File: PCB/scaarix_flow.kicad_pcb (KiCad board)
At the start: 2 copper layers, 153.4 x 160 mm, 63 parts

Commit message: Changed footprint and rerouted
Used a different footprint that wasn't hotswappable. Changed it and Re-routed
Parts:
- S1, S10, S11, S12, S13, S14, S15, S16, S17, S18, S19, S2, S20, S21, S22, S23, S24, S27, S3, S4, S5, S6, S7, S8, S9: footprint Erics_Footprints:SW_MX_reversible -> Erics_Footprints:MX_Hotswap
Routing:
- net P21: track 187.2 -> 243.5 mm, vias 0 -> 9
- net P19: track 145.2 -> 199.3 mm, vias 0 -> 5
- net P20: track 166.0 -> 219.2 mm, vias 0 -> 5
- net P18: track 126.8 -> 178.8 mm, vias 0 -> 5
- net P15: track 107.9 -> 159.9 mm, vias 0 -> 5
- net P14: track 89.2 -> 139.3 mm, vias 0 -> 10
- net ring_bottom: track 18.8 -> 44.7 mm, vias 0 -> 1
- net far_bottom: track 18.8 -> 44.7 mm, vias 0 -> 1
- net middle_top: track 18.8 -> 44.7 mm, vias 0 -> 1
- net ring_top: track 18.8 -> 44.7 mm, vias 0 -> 1
- net ring_home: track 18.8 -> 44.7 mm, vias 0 -> 1
- net middle_bottom: track 18.8 -> 44.7 mm, vias 0 -> 1
- net middle_home: track 18.8 -> 44.7 mm, vias 0 -> 1
- net far_home: track 18.8 -> 44.7 mm, vias 0 -> 1
- net far_top: track 18.8 -> 44.7 mm, vias 0 -> 1
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
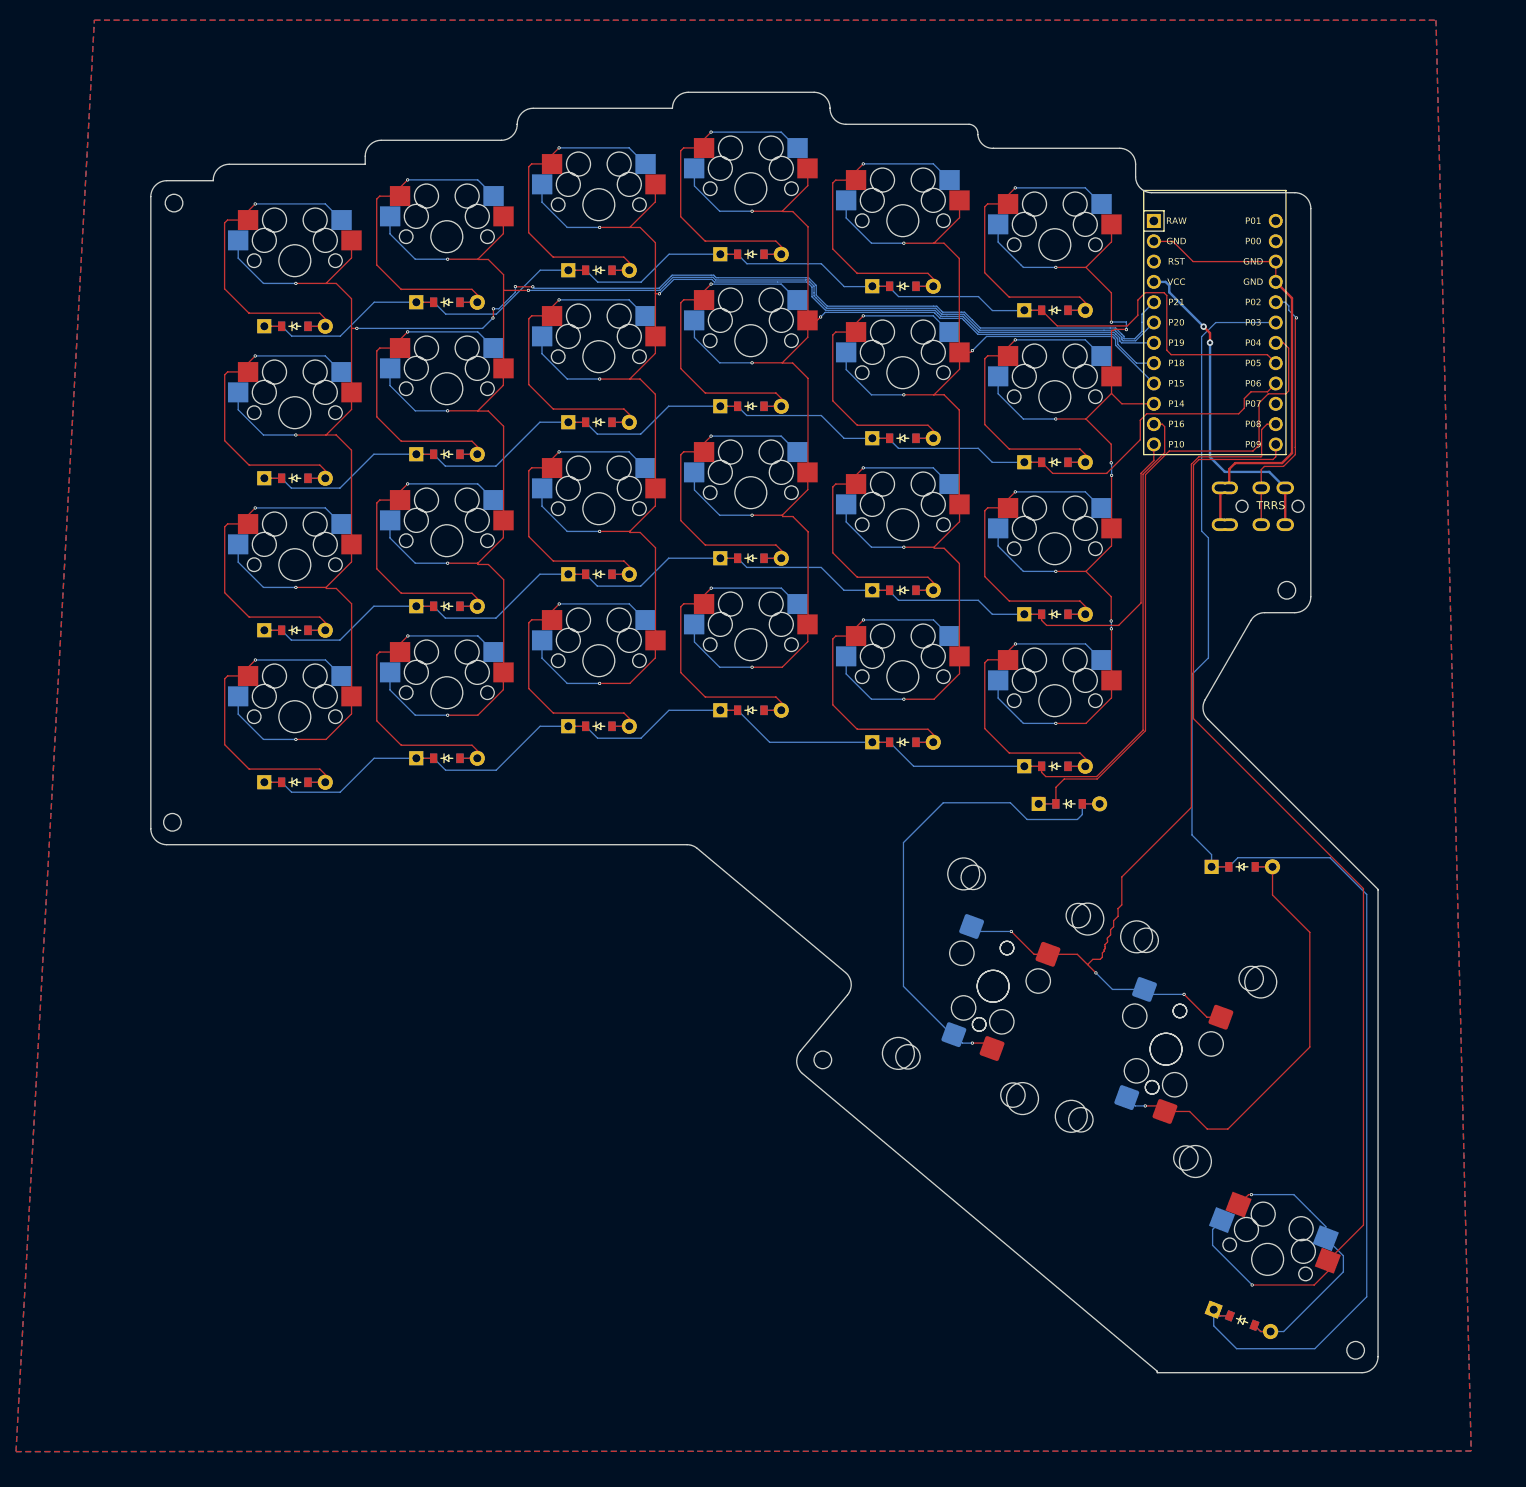
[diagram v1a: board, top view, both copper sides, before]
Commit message: Fixed stabilizers
Stab orientation was wrong
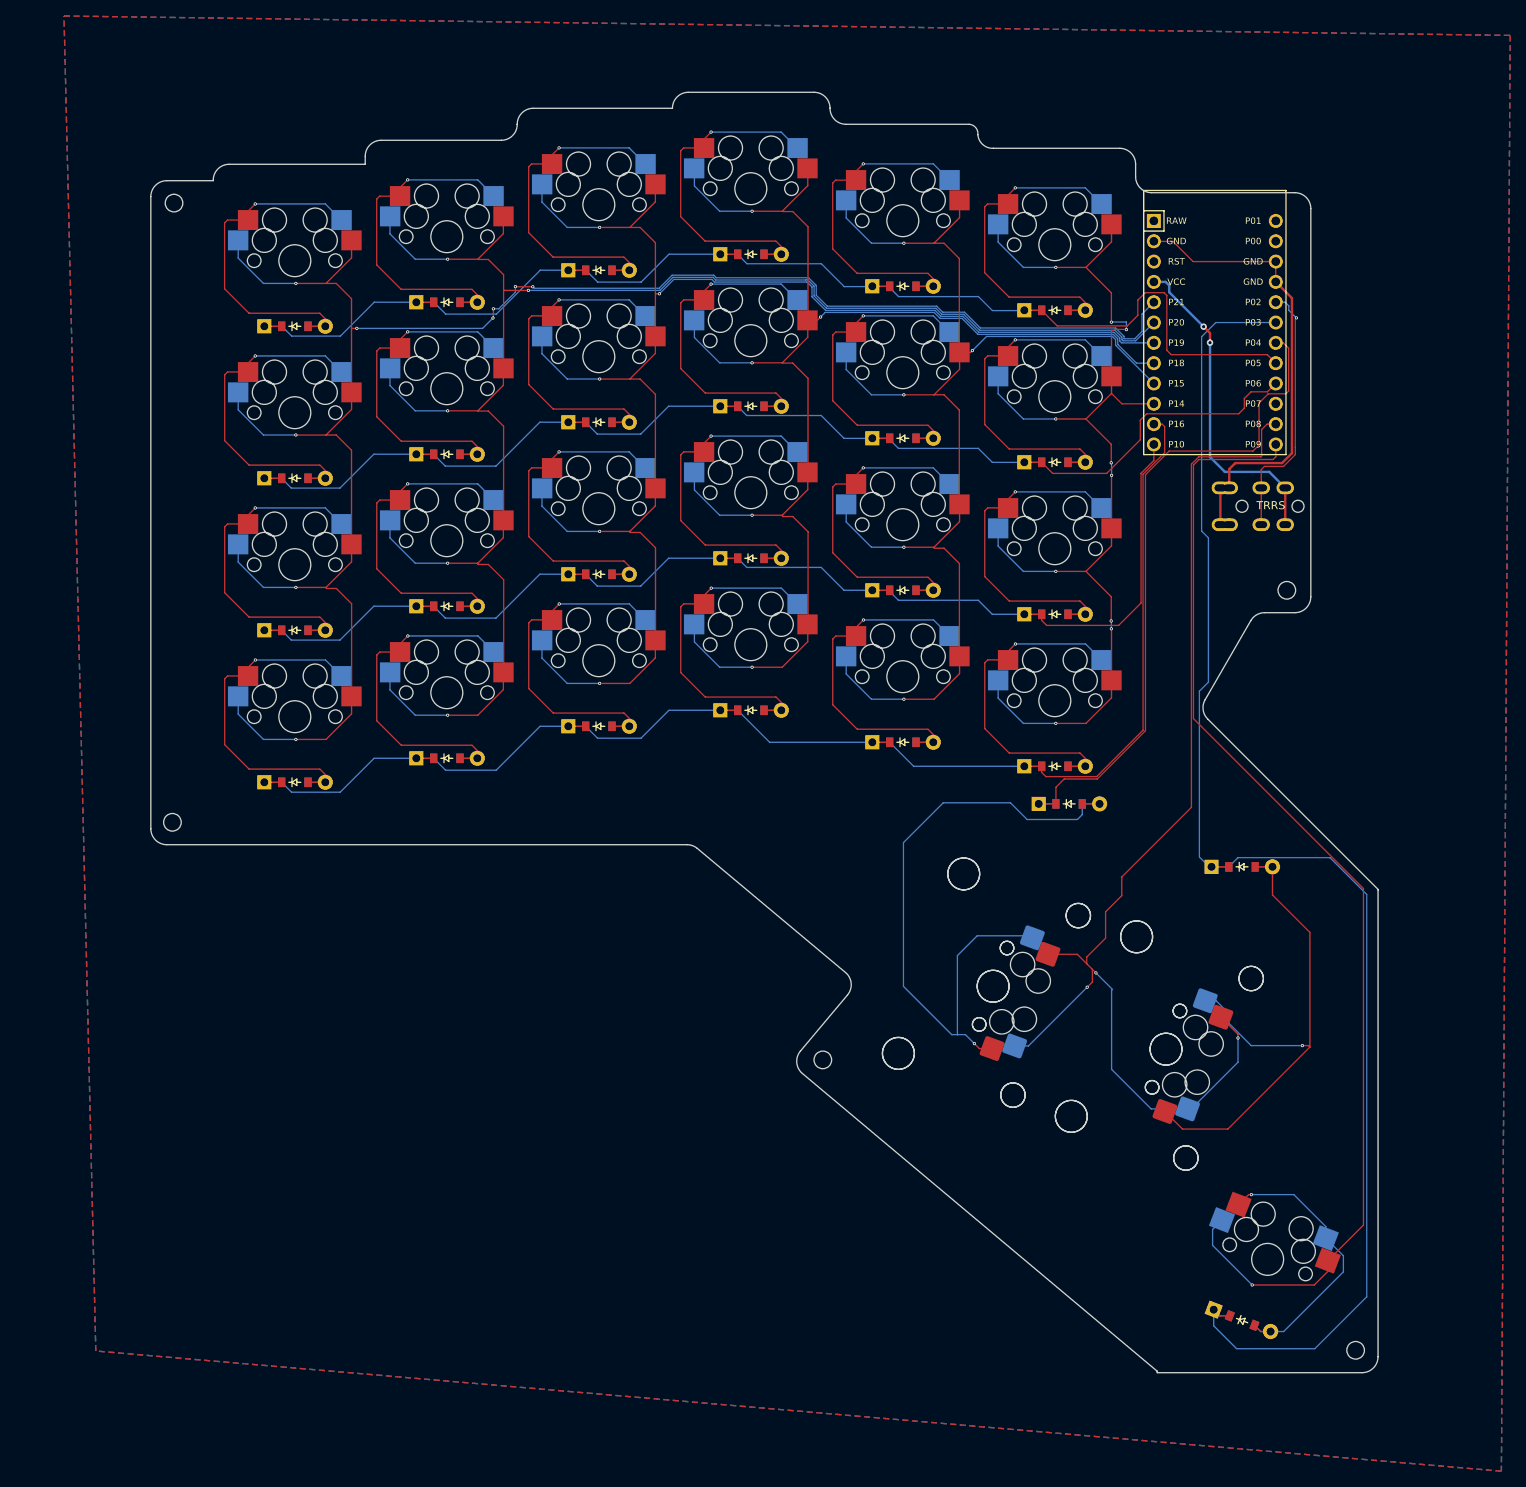
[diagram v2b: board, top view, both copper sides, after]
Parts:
- turned S25 to 70 degrees
- turned S26 to 70 degrees
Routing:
- net P8: track 118.9 -> 143.7 mm
- net 1_bottom: track 63.5 -> 83.8 mm
- net 1_top: track 57.6 -> 68.3 mm
